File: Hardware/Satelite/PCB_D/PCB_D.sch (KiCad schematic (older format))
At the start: 29 parts, among them J1 Conn_01x03, J2 Conector_Expansion_CanSat, J3 Conn_02x03_Odd_Even, J4 USB_B_Micro, M1 Spacer, M2 Spacer, M3 Spacer, SW1 Reset Switch, U1 ATmega328P-AU, U2 CSTNE16M0V530000R0, U3 FT231XS, U4 TPD2E2U06

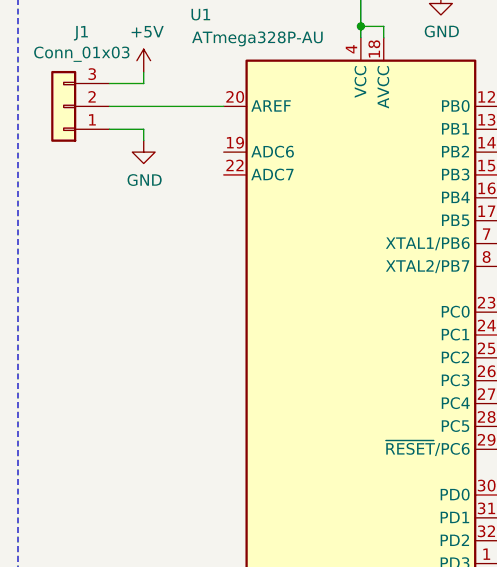
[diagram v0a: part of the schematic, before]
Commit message: Agregados logos en PCB_D y headers con tx y rx para debug
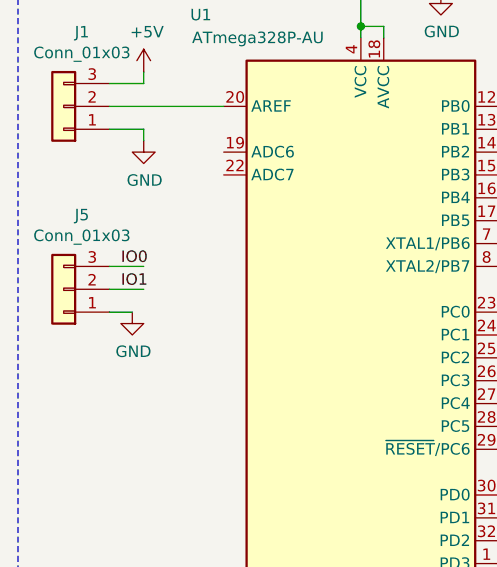
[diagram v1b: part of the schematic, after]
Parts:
- added J5: Conn_01x03, Connector_PinHeader_2.54mm:PinHeader_1x03_P2.54mm_Vertical, symbol Connector_Generic:Conn_01x03
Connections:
- wire segments 142 -> 145
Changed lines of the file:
@@
 Text Label 9700 3650 0    50   ~ 0
 D-
+$Comp
+L Connector_Generic:Conn_01x03 J5
+U 1 1 5BE50609
+P 850 5500
+F 0 "J5" H 770 5175 50  0000 C CNN
+F 1 "Conn_01x03" H 770 5266 50  0000 C CNN
+F 2 "Connector_PinHeader_2.54mm:PinHeader_1x03_P2.54mm_Vertical" H 850 5500 50  0001 C CNN
+F 3 "~" H 850 5500 50  0001 C CNN
+F 4 "61300311121" H 850 5500 50  0001 C CNN "Manufacturer Part Number"
+	1    850  5500
+	-1   0    0    1
+$EndComp
+$Comp
+L power:GND #PWR0102
+U 1 1 5BE5760B
+P 1150 5600
+F 0 "#PWR0102" H 1150 5350 50  0001 C CNN
+F 1 "GND" H 1155 5427 50  0000 C CNN
+F 2 "" H 1150 5600 50  0001 C CNN
+F 3 "" H 1150 5600 50  0001 C CNN
+	1    1150 5600
+	1    0    0    -1
+$EndComp
+Wire Wire Line
+	1050 5600 1150 5600
+Wire Wire Line
+	1050 5500 1200 5500
+Wire Wire Line
+	1050 5400 1200 5400
+Text Label 1100 5400 0    50   ~ 0
+IO0
+Text Label 1100 5500 0    50   ~ 0
+IO1
 $EndSCHEMATC

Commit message: BOM y corrección de footprint en PCB_D
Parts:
- U4: footprint SamacSys_Parts:SOT95P280X100-5N -> Package_TO_SOT_SMD:SOT-553; Manufacturer Part Number (none) -> TPD2E2U06DRLR
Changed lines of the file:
@@
 F 0 "U4" H 10400 3850 50  0000 L CNN
 F 1 "TPD2E2U06" H 10400 3750 50  0000 L CNN
-F 2 "SamacSys_Parts:SOT95P280X100-5N" H 9350 3500 50  0001 C CNN
+F 2 "Package_TO_SOT_SMD:SOT-553" H 9350 3500 50  0001 C CNN
 F 3 "http://www.ti.com/lit/ds/symlink/tpd2e2u06.pdf" H 9950 3950 50  0001 C CNN
+F 4 "TPD2E2U06DRLR" H 10150 3750 50  0001 C CNN "Manufacturer Part Number"
 	1    10150 3750
 	1    0    0    -1

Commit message: Permitir carga de la batería desde el USB de PCB_D
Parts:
- removed D4: LL4148, Diode_SMD:D_MiniMELF, symbol Diode:LL4148
- added D4: 1N4007, Diode_SMD:D_SMA, symbol Diode:1N4007
- U3: symbol Interface_USB:FT231XS -> PCB_D-rescue:FT231XS-Interface_USB
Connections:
- net labels added: VBUS
- wire segments 145 -> 144
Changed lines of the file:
@@
 $EndBitmap
 $Comp
-L Interface_USB:FT231XS U3
+L PCB_D-rescue:FT231XS-Interface_USB U3
 U 1 1 5BBD709B
 P 8750 3000
@@
 	2500 3900 2900 3900
 Connection ~ 2150 3900
-Text Label 3150 2000 0    50   ~ 0
+Text Label 4900 6300 0    50   ~ 0
 IO6
 Text Label 3150 2100 0    50   ~ 0
 IO7
-Text Label 3150 1400 0    50   ~ 0
-IO0
-Text Label 3150 1500 0    50   ~ 0
+Text Label 3150 1600 0    50   ~ 0
 IO1
-Text Label 3150 1600 0    50   ~ 0
+Text Label 3150 1700 0    50   ~ 0
 IO2
-Text Label 3150 1700 0    50   ~ 0
+Text Label 3150 1800 0    50   ~ 0
 IO3
-Text Label 3150 1800 0    50   ~ 0
+Text Label 3150 1900 0    50   ~ 0
 IO4
-Text Label 3150 1900 0    50   ~ 0
+Text Label 3150 2000 0    50   ~ 0
 IO5
 Text Label 3150 2450 0    50   ~ 0
@@
 $EndComp
 Wire Wire Line
-	3100 1400 3300 1400
-Wire Wire Line
 	3100 1500 3300 1500
 Wire Wire Line
@@
 Wire Wire Line
 	4900 7100 4900 7000
-Text Label 4900 6300 0    50   ~ 0
-SCK
 $Comp
 L Connector_Generic:Conn_01x03 J1
@@
 Wire Wire Line
 	1700 1450 1800 1450
-$Comp
-L power:+5V #PWR021
-U 1 1 5BE24D5E
-P 7500 1250
-F 0 "#PWR021" H 7500 1100 50  0001 C CNN
-F 1 "+5V" H 7514 1425 50  0000 C CNN
-F 2 "" H 7500 1250 50  0001 C CNN
-F 3 "" H 7500 1250 50  0001 C CNN
-	1    7500 1250
-	1    0    0    -1
-$EndComp
 Wire Wire Line
 	7050 1500 8850 1500
-Wire Wire Line
-	7350 1250 7500 1250
-Wire Wire Line
-	7050 1250 7050 1500
-Connection ~ 7050 1500
-$Comp
-L Diode:LL4148 D4
-U 1 1 5BE5040B
-P 7200 1250
-F 0 "D4" H 7200 1034 50  0000 C CNN
-F 1 "LL4148" H 7200 1125 50  0000 C CNN
-F 2 "Diode_SMD:D_MiniMELF" H 7200 1075 50  0001 C CNN
-F 3 "http://www.vishay.com/docs/85557/ll4148.pdf" H 7200 1250 50  0001 C CNN
-F 4 "LL4148-GS08" H 7200 1250 50  0001 C CNN "Manufacturer Part Number"
-	1    7200 1250
-	-1   0    0    1
-$EndComp
 $Comp
 L AXTEC_IC:Spacer M1
@@
 Text Label 1100 5500 0    50   ~ 0
 IO1
+$Comp
+L power:VBUS #PWR0103
+U 1 1 5C267EA8
+P 7050 1100
+F 0 "#PWR0103" H 7050 950 50  0001 C CNN
+F 1 "VBUS" H 7064 1275 50  0000 C CNN
+F 2 "" H 7050 1100 50  0001 C CNN
+F 3 "" H 7050 1100 50  0001 C CNN
+	1    7050 1100
+	1    0    0    -1
+$EndComp
+Wire Wire Line
+	7050 1400 7050 1500
+Connection ~ 7050 1500
+$Comp
+L power:VBUS #PWR0104
+U 1 1 5C275E4D
+P 3450 1400
+F 0 "#PWR0104" H 3450 1250 50  0001 C CNN
+F 1 "VBUS" H 3464 1575 50  0000 C CNN
+F 2 "" H 3450 1400 50  0001 C CNN
+F 3 "" H 3450 1400 50  0001 C CNN
+	1    3450 1400
+	1    0    0    -1
+$EndComp
+Wire Wire Line
+	3100 1400 3450 1400
+Text Label 3150 1500 0    50   ~ 0
+IO0
+$Comp
+L Diode:1N4007 D4
+U 1 1 5C28CCE7
+P 7050 1250
+F 0 "D4" V 7004 1329 50  0000 L CNN
+F 1 "1N4007" V 7096 1329 50  0000 L CNN
+F 2 "Diode_SMD:D_SMA" H 7050 1075 50  0001 C CNN
+F 3 "http://www.vishay.com/docs/88503/1n4001.pdf" H 7050 1250 50  0001 C CNN
+	1    7050 1250
+	0    1    1    0
+$EndComp
 $EndSCHEMATC

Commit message: Modificaciones en D6, D7 y serigrafia PCB_D
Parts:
- U3: symbol PCB_D-rescue:FT231XS-Interface_USB -> PCB_D-rescue:FT231XS-Interface_USB-PCB_D-rescue
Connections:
- net labels added: A0, A1, A2, A3, D0, D1, D2, D3, D4, D5, D6, D7, D8, D9
- net labels removed: AD0, AD1, AD2, AD3, IO0, IO1, IO2, IO3, IO4, IO5, IO6, IO7, IO8, IO9
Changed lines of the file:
@@
 $EndBitmap
 $Comp
-L PCB_D-rescue:FT231XS-Interface_USB U3
+L PCB_D-rescue:FT231XS-Interface_USB-PCB_D-rescue U3
 U 1 1 5BBD709B
 P 8750 3000
@@
 Conexión USB Arduino
 Text Label 2900 6500 0    50   ~ 0
-IO1
+D1
 $Comp
 L Device:R R3
@@
 $EndComp
 Text Label 2900 6400 0    50   ~ 0
-IO0
+D0
 Wire Wire Line
 	2750 6400 3600 6400
@@
 	2750 6600 3100 6600
 Text Label 2900 6600 0    50   ~ 0
-IO2
+D2
 $Comp
 L Device:R R2
@@
 	2750 6700 3100 6700
 Text Label 2900 6700 0    50   ~ 0
-IO3
+D3
 Text Label 2900 6800 0    50   ~ 0
-IO4
+D4
 Wire Wire Line
 	2750 6800 3100 6800
@@
 	2750 6900 3100 6900
 Text Label 2900 6900 0    50   ~ 0
-IO5
+D5
 Text Label 2900 7000 0    50   ~ 0
-IO6
+D6
 Wire Wire Line
 	2750 7000 3100 7000
@@
 	2750 7100 3100 7100
 Text Label 2900 7100 0    50   ~ 0
-IO7
+D7
 Wire Wire Line
 	2750 5600 3100 5600
@@
 	2750 6100 3250 6100
 Text Label 2900 5600 0    50   ~ 0
-AD0
+A0
 Text Label 2900 5700 0    50   ~ 0
-AD1
+A1
 Text Label 2900 5800 0    50   ~ 0
-AD2
+A2
 Text Label 2900 5900 0    50   ~ 0
-AD3
+A3
 Text Label 2900 6000 0    50   ~ 0
 SDA
@@
 	2750 5200 3300 5200
 Text Label 2900 4700 0    50   ~ 0
-IO8
+D8
 Text Label 2900 4800 0    50   ~ 0
-IO9
+D9
 Text Label 2900 4900 0    50   ~ 0
 SS
@@
 Connection ~ 2150 3900
 Text Label 4900 6300 0    50   ~ 0
-IO6
-Text Label 3150 2100 0    50   ~ 0
-IO7
+D7
 Text Label 3150 1600 0    50   ~ 0
-IO1
+D1
 Text Label 3150 1700 0    50   ~ 0
-IO2
+D2
 Text Label 3150 1800 0    50   ~ 0
-IO3
+D3
 Text Label 3150 1900 0    50   ~ 0
-IO4
+D4
 Text Label 3150 2000 0    50   ~ 0
-IO5
+D5
 Text Label 3150 2450 0    50   ~ 0
-AD0
+A0
 Text Label 3150 2550 0    50   ~ 0
-AD1
+A1
 Text Label 3150 2650 0    50   ~ 0
-AD2
+A2
 Text Label 3150 2750 0    50   ~ 0
-AD3
+A3
 $Comp
 L AXTEC_IC:Conector_Expansion_CanSat J2
@@
 	1050 5400 1200 5400
 Text Label 1100 5400 0    50   ~ 0
-IO0
+D0
 Text Label 1100 5500 0    50   ~ 0
-IO1
+D1
 $Comp
 L power:VBUS #PWR0103
@@
 	3100 1400 3450 1400
 Text Label 3150 1500 0    50   ~ 0
-IO0
+D0
 $Comp
 L Diode:1N4007 D4
@@
 	0    1    1    0
 $EndComp
+Text Label 3150 2100 0    50   ~ 0
+D6
 $EndSCHEMATC

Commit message: Nuevo circuito en PCB_D para permitir recepción desde el UART del ESP32 y del USB
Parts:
- removed R3: 1k, Resistor_SMD:R_0603_1608Metric_Pad1.05x0.95mm_HandSolder, symbol Device:R
- added D5, D6: 1N4148, Diode_SMD:D_MiniMELF, symbol Diode:1N4148
- R1: value 1k -> 100k; Manufacturer Part Number RC0603JR-071KL -> RC0603JR-07100KL
- U3: symbol PCB_D-rescue:FT231XS-Interface_USB-PCB_D-rescue -> PCB_D-rescue:FT231XS-Interface_USB-PCB_D-rescue-PCB_D-rescue
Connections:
- net labels added: TX_ESP32, TX_USB
- net labels removed: D0, D1
- wire segments 144 -> 151
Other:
- moved on the sheet: D1, R4
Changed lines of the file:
@@
 $EndBitmap
 $Comp
-L PCB_D-rescue:FT231XS-Interface_USB-PCB_D-rescue U3
+L PCB_D-rescue:FT231XS-Interface_USB-PCB_D-rescue-PCB_D-rescue U3
 U 1 1 5BBD709B
 P 8750 3000
@@
 TXD
 Text Label 7700 2400 0    50   ~ 0
-RXD
+TX_USB
 Text Label 7700 2800 0    50   ~ 0
 DTR
 Text Notes 8800 1000 0    118  ~ 0
 Conexión USB Arduino
-Text Label 2900 6500 0    50   ~ 0
-D1
-$Comp
-L Device:R R3
-U 1 1 5BC06911
-P 3750 6400
-F 0 "R3" V 3850 6400 50  0000 C CNN
-F 1 "1k" V 3634 6400 50  0000 C CNN
-F 2 "Resistor_SMD:R_0603_1608Metric_Pad1.05x0.95mm_HandSolder" V 3680 6400 50  0001 C CNN
-F 3 "~" H 3750 6400 50  0001 C CNN
-F 4 "RC0603JR-071KL" V 3750 6400 50  0001 C CNN "Manufacturer Part Number"
-	1    3750 6400
-	0    1    1    0
-$EndComp
-Text Label 2900 6400 0    50   ~ 0
-D0
-Wire Wire Line
-	2750 6400 3600 6400
-Text Label 4200 6400 0    50   ~ 0
-RXD
-Wire Wire Line
-	3900 6400 4400 6400
 Wire Wire Line
 	2750 6600 3100 6600
@@
 	1    0    0    -1
 $EndComp
-$Comp
-L Device:R R1
-U 1 1 5BC72B6F
-P 3450 6500
-F 0 "R1" V 3550 6500 50  0000 C CNN
-F 1 "1k" V 3334 6500 50  0000 C CNN
-F 2 "Resistor_SMD:R_0603_1608Metric_Pad1.05x0.95mm_HandSolder" V 3380 6500 50  0001 C CNN
-F 3 "~" H 3450 6500 50  0001 C CNN
-F 4 "RC0603JR-071KL" V 3450 6500 50  0001 C CNN "Manufacturer Part Number"
-	1    3450 6500
-	0    1    1    0
-$EndComp
-Wire Wire Line
-	2750 6500 3300 6500
-Wire Wire Line
-	3600 6500 4400 6500
-Text Label 4200 6500 0    50   ~ 0
+Text Label 2900 6500 0    50   ~ 0
 TXD
 $Comp
@@
 	2500 3900 2900 3900
 Connection ~ 2150 3900
-Text Label 4900 6300 0    50   ~ 0
+Text Label 5050 6250 0    50   ~ 0
 D7
-Text Label 3150 1600 0    50   ~ 0
-D1
 Text Label 3150 1700 0    50   ~ 0
 D2
@@
 $EndComp
 Wire Wire Line
-	3100 1500 3300 1500
+	3100 1500 3550 1500
 Wire Wire Line
 	3100 1600 3300 1600
@@
 Connection ~ 8850 1500
 Wire Wire Line
-	4900 6300 4900 6350
+	5050 6250 5050 6300
 $Comp
 L Device:LED D?
 U 1 1 5BC9091B
-P 4900 6850
+P 5050 6800
 AR Path="/5B9997DB/5BC9091B" Ref="D?"  Part="1"
 AR Path="/5BC9091B" Ref="D1"  Part="1"
-F 0 "D1" V 4938 6733 50  0000 R CNN
-F 1 "Verde" V 4847 6733 50  0000 R CNN
-F 2 "LED_SMD:LED_0603_1608Metric" H 4900 6850 50  0001 C CNN
-F 3 "~" H 4900 6850 50  0001 C CNN
-F 4 "150060VS75000" V 4900 6850 50  0001 C CNN "Manufacturer Part Number"
-	1    4900 6850
+F 0 "D1" V 5088 6683 50  0000 R CNN
+F 1 "Verde" V 4997 6683 50  0000 R CNN
+F 2 "LED_SMD:LED_0603_1608Metric" H 5050 6800 50  0001 C CNN
+F 3 "~" H 5050 6800 50  0001 C CNN
+F 4 "150060VS75000" V 5050 6800 50  0001 C CNN "Manufacturer Part Number"
+	1    5050 6800
 	0    -1   -1   0
 $EndComp
 Wire Wire Line
-	4900 6700 4900 6650
+	5050 6650 5050 6600
 $Comp
 L power:GND #PWR013
 U 1 1 5BC96C3C
-P 4900 7100
-F 0 "#PWR013" H 4900 6850 50  0001 C CNN
-F 1 "GND" H 4904 6926 50  0000 C CNN
-F 2 "" H 4900 7100 50  0001 C CNN
-F 3 "" H 4900 7100 50  0001 C CNN
-	1    4900 7100
-	1    0    0    -1
-$EndComp
-Wire Wire Line
-	4900 7100 4900 7000
+P 5050 7050
+F 0 "#PWR013" H 5050 6800 50  0001 C CNN
+F 1 "GND" H 5054 6876 50  0000 C CNN
+F 2 "" H 5050 7050 50  0001 C CNN
+F 3 "" H 5050 7050 50  0001 C CNN
+	1    5050 7050
+	1    0    0    -1
+$EndComp
+Wire Wire Line
+	5050 7050 5050 6950
 $Comp
 L Connector_Generic:Conn_01x03 J1
@@
 L Device:R R?
 U 1 1 5C2EDFB7
-P 4900 6500
+P 5050 6450
 AR Path="/5B9997DB/5C2EDFB7" Ref="R?"  Part="1"
 AR Path="/5C2EDFB7" Ref="R4"  Part="1"
-F 0 "R4" H 4970 6546 50  0000 L CNN
-F 1 "220" H 4970 6455 50  0000 L CNN
-F 2 "Resistor_SMD:R_0603_1608Metric_Pad1.05x0.95mm_HandSolder" V 4830 6500 50  0001 C CNN
-F 3 "~" H 4900 6500 50  0001 C CNN
-F 4 "RC0603JR-13220RL" H 4900 6500 50  0001 C CNN "Manufacturer Part Number"
-	1    4900 6500
+F 0 "R4" H 5120 6496 50  0000 L CNN
+F 1 "220" H 5120 6405 50  0000 L CNN
+F 2 "Resistor_SMD:R_0603_1608Metric_Pad1.05x0.95mm_HandSolder" V 4980 6450 50  0001 C CNN
+F 3 "~" H 5050 6450 50  0001 C CNN
+F 4 "RC0603JR-13220RL" H 5050 6450 50  0001 C CNN "Manufacturer Part Number"
+	1    5050 6450
 	1    0    0    -1
 $EndComp
@@
 Wire Wire Line
 	1050 5400 1200 5400
-Text Label 1100 5400 0    50   ~ 0
-D0
-Text Label 1100 5500 0    50   ~ 0
-D1
 $Comp
 L power:VBUS #PWR0103
@@
 Wire Wire Line
 	3100 1400 3450 1400
-Text Label 3150 1500 0    50   ~ 0
-D0
 $Comp
 L Diode:1N4007 D4
@@
 Text Label 3150 2100 0    50   ~ 0
 D6
+$Comp
+L Diode:1N4148 D5
+U 1 1 5C2DE090
+P 4050 6700
+F 0 "D5" H 4050 6917 50  0000 C CNN
+F 1 "1N4148" H 4050 6825 50  0000 C CNN
+F 2 "Diode_SMD:D_MiniMELF" H 4050 6525 50  0001 C CNN
+F 3 "https://www.vishay.com/docs/85561/ls4148.pdf" H 4050 6700 50  0001 C CNN
+F 4 "LS4148-GS08" H 4050 6700 50  0001 C CNN "Manufacturer Part Number"
+	1    4050 6700
+	1    0    0    -1
+$EndComp
+$Comp
+L Diode:1N4148 D6
+U 1 1 5C2DE493
+P 4050 6900
+F 0 "D6" H 4050 6800 50  0000 C CNN
+F 1 "1N4148" H 4050 6700 50  0000 C CNN
+F 2 "Diode_SMD:D_MiniMELF" H 4050 6725 50  0001 C CNN
+F 3 "https://www.vishay.com/docs/85561/ls4148.pdf" H 4050 6900 50  0001 C CNN
+F 4 "LS4148-GS08" H 4050 6900 50  0001 C CNN "Manufacturer Part Number"
+	1    4050 6900
+	1    0    0    -1
+$EndComp
+Wire Wire Line
+	2750 6500 3100 6500
+Text Label 3150 1600 0    50   ~ 0
+TXD
+Text Label 3150 1500 0    50   ~ 0
+TX_ESP32
+Text Label 1200 5400 2    50   ~ 0
+RXD
+Text Label 1200 5500 2    50   ~ 0
+TXD
+$Comp
+L Device:R R1
+U 1 1 5C30FBC4
+P 3600 6700
+F 0 "R1" V 3700 6700 50  0000 C CNN
+F 1 "100k" V 3484 6700 50  0000 C CNN
+F 2 "Resistor_SMD:R_0603_1608Metric_Pad1.05x0.95mm_HandSolder" V 3530 6700 50  0001 C CNN
+F 3 "~" H 3600 6700 50  0001 C CNN
+F 4 "RC0603JR-07100KL" V 3600 6700 50  0001 C CNN "Manufacturer Part Number"
+	1    3600 6700
+	-1   0    0    1
+$EndComp
+Wire Wire Line
+	2750 6400 3250 6400
+Wire Wire Line
+	3900 6900 3850 6900
+Wire Wire Line
+	3250 6900 3250 6400
+Wire Wire Line
+	3900 6700 3850 6700
+Wire Wire Line
+	3850 6700 3850 6900
+Connection ~ 3850 6900
+Text Label 4250 6700 0    50   ~ 0
+TX_USB
+Text Label 4250 6900 0    50   ~ 0
+TX_ESP32
+Wire Wire Line
+	4200 6900 4650 6900
+Wire Wire Line
+	4200 6700 4650 6700
+Wire Wire Line
+	3600 6900 3600 6850
+Wire Wire Line
+	3250 6900 3600 6900
+Connection ~ 3600 6900
+Wire Wire Line
+	3600 6900 3850 6900
+$Comp
+L power:+5V #PWR021
+U 1 1 5C379480
+P 3600 6550
+F 0 "#PWR021" H 3600 6400 50  0001 C CNN
+F 1 "+5V" H 3614 6725 50  0000 C CNN
+F 2 "" H 3600 6550 50  0001 C CNN
+F 3 "" H 3600 6550 50  0001 C CNN
+	1    3600 6550
+	1    0    0    -1
+$EndComp
+Text Label 3050 6400 2    50   ~ 0
+RXD
 $EndSCHEMATC

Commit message: Agregado pull-up para CBUS3 del FT231XS faltante y corregido D+ y D- invertidos en PCB_D
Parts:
- added R3: 10k, Resistor_SMD:R_0603_1608Metric_Pad1.05x0.95mm_HandSolder, symbol Device:R
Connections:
- wire segments 151 -> 161
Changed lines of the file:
@@
 	1    0    0    -1
 $EndComp
-Wire Wire Line
-	9850 2700 9450 2700
-Wire Wire Line
-	9850 2800 9450 2800
 $Comp
 L power:GND #PWR020
@@
 Wire Wire Line
 	10150 4100 10150 4050
-Text Label 9650 2700 0    50   ~ 0
-D+
-Text Label 9650 2800 0    50   ~ 0
-D-
 Wire Wire Line
 	9850 3650 9700 3650
@@
 Text Label 3050 6400 2    50   ~ 0
 RXD
+$Comp
+L Device:R R3
+U 1 1 5C2E87A0
+P 7300 3950
+F 0 "R3" H 7230 3904 50  0000 R CNN
+F 1 "10k" H 7230 3996 50  0000 R CNN
+F 2 "Resistor_SMD:R_0603_1608Metric_Pad1.05x0.95mm_HandSolder" V 7230 3950 50  0001 C CNN
+F 3 "~" H 7300 3950 50  0001 C CNN
+F 4 "RC0603JR-0710KL" H 7300 3950 50  0001 C CNN "Manufacturer Part Number"
+	1    7300 3950
+	1    0    0    -1
+$EndComp
+$Comp
+L power:VBUS #PWR0105
+U 1 1 5C2E8CBB
+P 7300 3800
+F 0 "#PWR0105" H 7300 3650 50  0001 C CNN
+F 1 "VBUS" H 7314 3975 50  0000 C CNN
+F 2 "" H 7300 3800 50  0001 C CNN
+F 3 "" H 7300 3800 50  0001 C CNN
+	1    7300 3800
+	1    0    0    -1
+$EndComp
+Wire Wire Line
+	7300 4100 7300 4200
+Wire Wire Line
+	7300 4200 7900 4200
+Wire Wire Line
+	7900 4200 7900 3600
+Wire Wire Line
+	7900 3600 8050 3600
+Wire Wire Line
+	9450 2700 9750 2700
+Wire Wire Line
+	9750 2700 9750 2800
+Wire Wire Line
+	9750 2800 9850 2800
+Wire Wire Line
+	9850 2700 9800 2700
+Wire Wire Line
+	9800 2700 9800 2750
+Wire Wire Line
+	9800 2750 9700 2750
+Wire Wire Line
+	9700 2750 9700 2800
+Wire Wire Line
+	9700 2800 9450 2800
+Text Label 9600 2700 0    50   ~ 0
+D-
+Text Label 9600 2800 0    50   ~ 0
+D+
 $EndSCHEMATC

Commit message: Logo open hardware en esquemáticos
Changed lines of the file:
@@
 Text Label 9600 2800 0    50   ~ 0
 D+
+$Comp
+L Graphic:Logo_Open_Hardware_Large #LOGO?
+U 1 1 5C3319FC
+P 8750 5500
+F 0 "#LOGO?" H 8750 6000 50  0001 C CNN
+F 1 "Logo_Open_Hardware_Large" H 8750 5100 50  0001 C CNN
+F 2 "" H 8750 5500 50  0001 C CNN
+F 3 "~" H 8750 5500 50  0001 C CNN
+	1    8750 5500
+	1    0    0    -1
+$EndComp
 $EndSCHEMATC

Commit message: Pequeña modificacion en PCB_D
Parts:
- U3: symbol PCB_D-rescue:FT231XS-Interface_USB-PCB_D-rescue-PCB_D-rescue -> PCB_D-rescue:FT231XS-Interface_USB-PCB_D-rescue-PCB_D-rescue-PCB_D-rescue
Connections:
- wire segments 161 -> 157
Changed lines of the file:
@@
 $EndBitmap
 $Comp
-L PCB_D-rescue:FT231XS-Interface_USB-PCB_D-rescue-PCB_D-rescue U3
+L PCB_D-rescue:FT231XS-Interface_USB-PCB_D-rescue-PCB_D-rescue-PCB_D-rescue U3
 U 1 1 5BBD709B
 P 8750 3000
@@
 	10150 3150 10150 3100
 Wire Wire Line
-	9450 2400 9550 2400
-Wire Wire Line
-	9450 3000 9550 3000
-Wire Wire Line
 	9750 1500 9750 2500
 Wire Wire Line
@@
 	8850 1500 8850 2100
 Wire Wire Line
-	9550 2000 8650 2000
-Wire Wire Line
 	8650 2000 8650 2100
-Wire Wire Line
-	9550 2000 9550 2400
 Connection ~ 9000 1500
 Wire Wire Line
 	9000 1500 9400 1500
-Wire Wire Line
-	9550 3000 9550 2400
-Connection ~ 9550 2400
 $Comp
 L Device:C_Small C5
@@
 Wire Wire Line
 	7900 3600 8050 3600
-Wire Wire Line
-	9450 2700 9750 2700
-Wire Wire Line
-	9750 2700 9750 2800
-Wire Wire Line
-	9750 2800 9850 2800
-Wire Wire Line
-	9850 2700 9800 2700
-Wire Wire Line
-	9800 2700 9800 2750
-Wire Wire Line
-	9800 2750 9700 2750
-Wire Wire Line
-	9700 2750 9700 2800
-Wire Wire Line
-	9700 2800 9450 2800
-Text Label 9600 2700 0    50   ~ 0
+Text Label 9450 2700 0    50   ~ 0
 D-
-Text Label 9600 2800 0    50   ~ 0
+Text Label 9450 2800 0    50   ~ 0
 D+
 $Comp
@@
 	1    0    0    -1
 $EndComp
+Wire Wire Line
+	9450 2700 9500 2700
+Wire Wire Line
+	9450 2800 9500 2800
+Wire Wire Line
+	9600 2000 9600 2400
+Wire Wire Line
+	9450 3000 9600 3000
+Wire Wire Line
+	8650 2000 9600 2000
+Wire Wire Line
+	9450 2400 9600 2400
+Connection ~ 9600 2400
+Wire Wire Line
+	9600 2400 9600 3000
+Text Label 9750 2700 0    50   ~ 0
+D+
+Text Label 9750 2800 0    50   ~ 0
+D-
+Wire Wire Line
+	9750 2700 9850 2700
+Wire Wire Line
+	9750 2800 9850 2800
 $EndSCHEMATC
